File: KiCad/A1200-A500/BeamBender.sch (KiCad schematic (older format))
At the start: 17 parts, among them J1 4-1734742-0, J2 HDMI_A_1.4, J3 STX-3501-3N, U1 LM1117-3.3, U3 ADV7513BSWZ

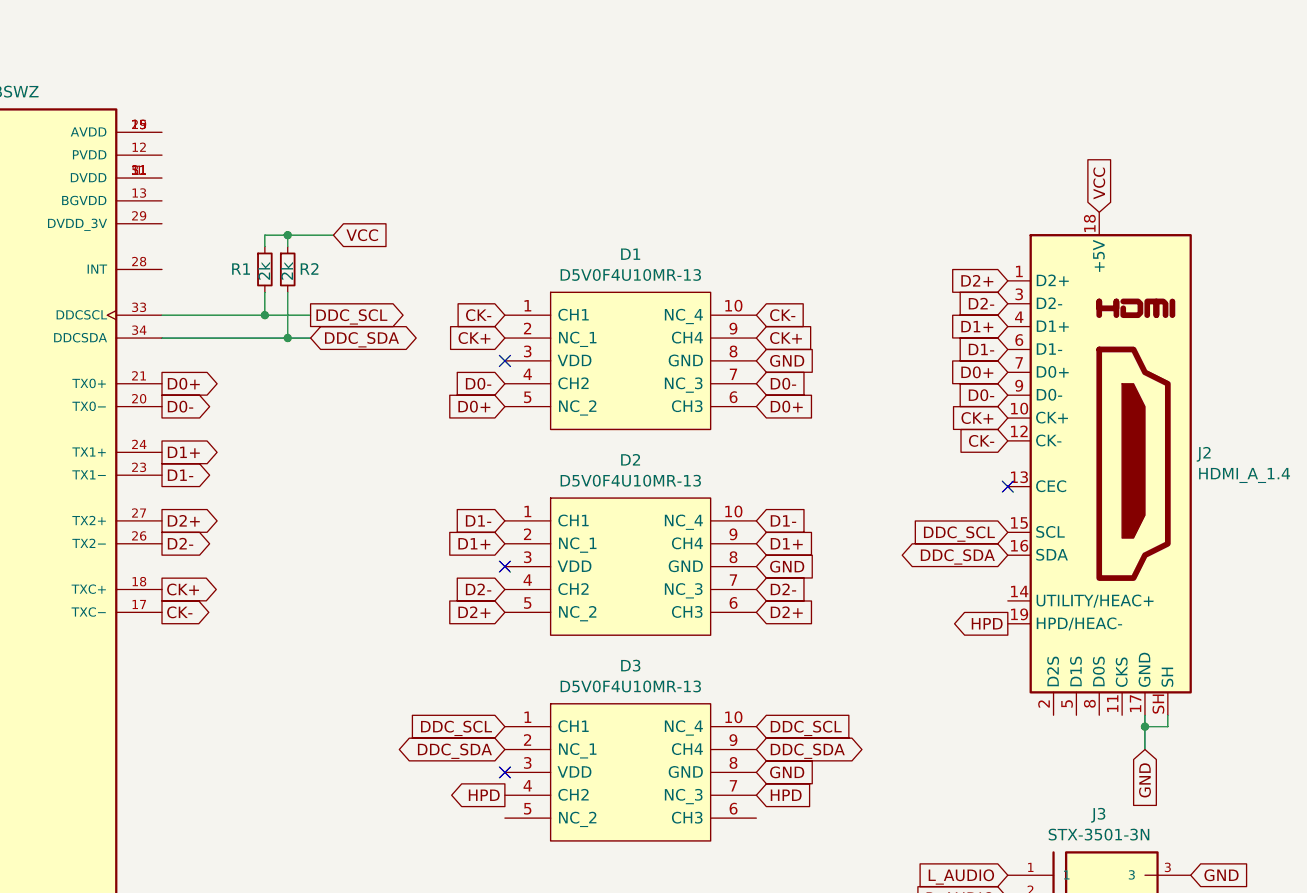
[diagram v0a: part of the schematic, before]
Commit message: more diff-pair routing
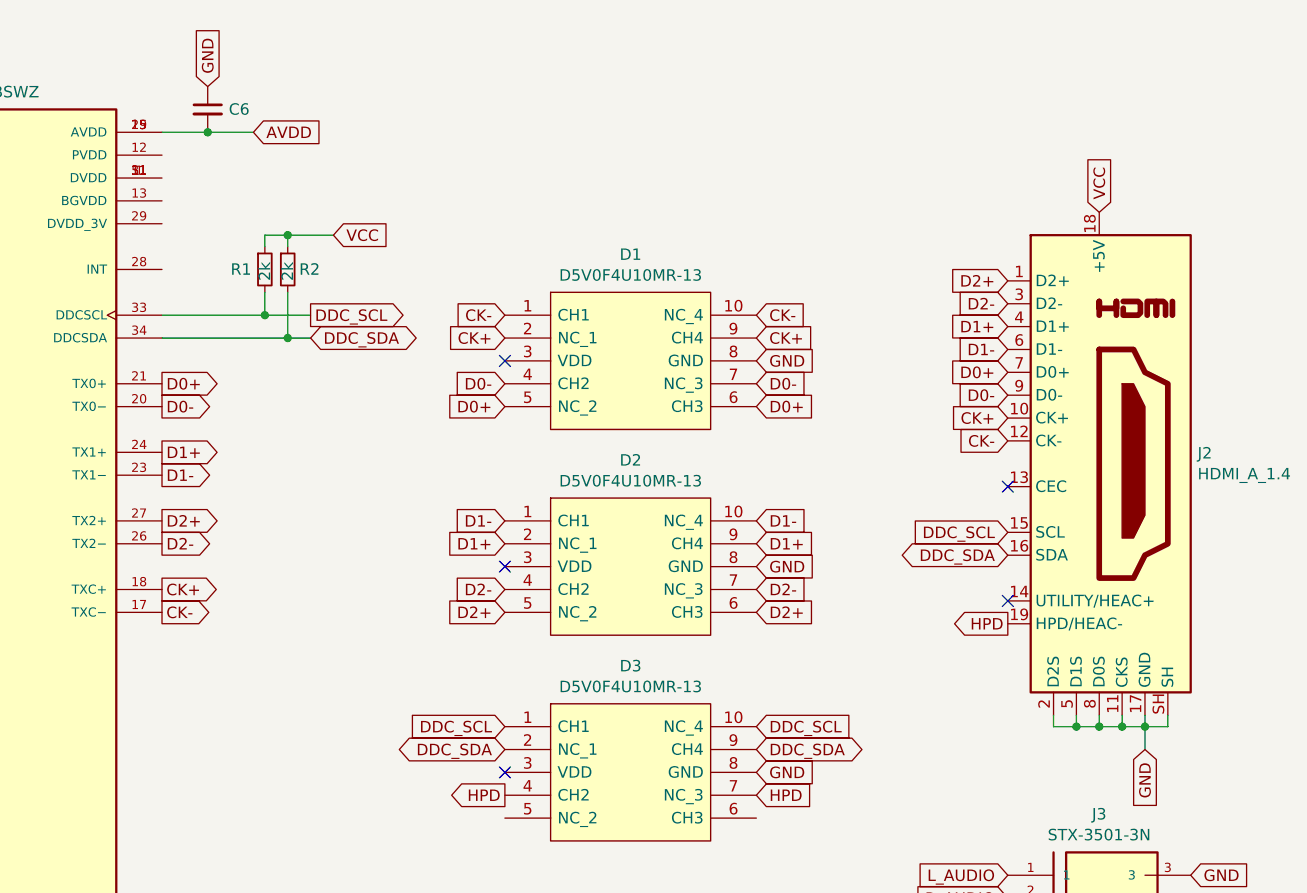
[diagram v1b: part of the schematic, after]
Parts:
- added C6: C_Small, Capacitor_SMD:C_0603_1608Metric_Pad1.08x0.95mm_HandSolder, symbol Device:C_Small
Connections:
- net GND: now also J2.11 (CKS), J2.2 (D2S), J2.5 (D1S), J2.8 (D0S), C6.1
- net AVDD: now reaches U3.15 (AVDD), U3.19 (AVDD), U3.25 (AVDD)
- net AVDD: now also C6.2
- no-connect marks 10 -> 11
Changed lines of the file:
@@
 Text GLabel 4400 5200 0    50   Input ~ 0
 R7_FPGA
+Wire Wire Line
+	9900 3450 9900 3500
+Wire Wire Line
+	9900 3500 10000 3500
+Wire Wire Line
+	10000 3450 10000 3500
+Connection ~ 10000 3500
+Wire Wire Line
+	10000 3500 10100 3500
+Wire Wire Line
+	10100 3450 10100 3500
+Connection ~ 10100 3500
+Wire Wire Line
+	10100 3500 10200 3500
+Wire Wire Line
+	10200 3450 10200 3500
+Connection ~ 10200 3500
+Wire Wire Line
+	10200 3500 10300 3500
+NoConn ~ 9700 2950
+Text GLabel 6400 900  2    50   Input ~ 0
+AVDD
+Wire Wire Line
+	6000 900  6200 900
+$Comp
+L Device:C_Small C6
+U 1 1 653C1DFE
+P 6200 800
+F 0 "C6" H 6292 800 50  0000 L CNN
+F 1 "C_Small" H 6292 755 50  0001 L CNN
+F 2 "Capacitor_SMD:C_0603_1608Metric_Pad1.08x0.95mm_HandSolder" H 6200 800 50  0001 C CNN
+F 3 "~" H 6200 800 50  0001 C CNN
+	1    6200 800
+	1    0    0    -1
+$EndComp
+Connection ~ 6200 900
+Wire Wire Line
+	6200 900  6400 900
+Text GLabel 6200 700  1    50   Input ~ 0
+GND
 $EndSCHEMATC

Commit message: more place and route
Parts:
- added C10, C11, C8, C9: 0.1uF, Capacitor_SMD:C_0603_1608Metric_Pad1.08x0.95mm_HandSolder, symbol Device:C_Small
- added C7: C_Small, Capacitor_SMD:C_0603_1608Metric_Pad1.08x0.95mm_HandSolder, symbol Device:C_Small
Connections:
- net labels added: Vp_D1, Vp_D2
- wire segments 58 -> 69
- no-connect marks 11 -> 10
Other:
- note added: "Central ESD clamp connected to VCC to \nalso provide protection for the VCC-line."
- note added: "ESD Protection"
- note added: "ESD bypass, \nThis limits any momentary voltage surge \nat the IO pin during the ESD strike event."
- moved on the sheet: D1, D2, D3
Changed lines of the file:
@@
 	1    0    0    -1
 $EndComp
-Text GLabel 10100 1250 1    50   Input ~ 0
+Text GLabel 10100 1150 2    50   Input ~ 0
 VCC
 Text GLabel 1150 2400 0    50   Input ~ 0
@@
 L BeamBender:D5V0F4U10MR-13 D1
 U 1 1 65246756
-P 8050 1900
-F 0 "D1" H 8050 2365 50  0000 C CNN
-F 1 "D5V0F4U10MR-13" H 8050 2274 50  0000 C CNN
-F 2 "BeamBender:SOP50P490X110-10N" H 8450 2200 50  0001 L CNN
-F 3 "" H 8450 2100 50  0001 L CNN
-	1    8050 1900
+P 8250 1800
+F 0 "D1" H 8250 1800 50  0000 C CNN
+F 1 "D5V0F4U10MR-13" H 8250 2174 50  0000 C CNN
+F 2 "BeamBender:SOP50P490X110-10N" H 8650 2100 50  0001 L CNN
+F 3 "" H 8650 2000 50  0001 L CNN
+	1    8250 1800
 	1    0    0    -1
 $EndComp
@@
 Text GLabel 6000 3000 2    50   Output ~ 0
 CK-
-Text GLabel 7500 1700 0    50   Input ~ 0
+Text GLabel 7700 1600 0    50   Input ~ 0
 CK-
-Text GLabel 7500 1800 0    50   Input ~ 0
+Text GLabel 7700 1700 0    50   Input ~ 0
 CK+
-Text GLabel 8600 1700 2    50   Input ~ 0
+Text GLabel 8800 1600 2    50   Input ~ 0
 CK-
-Text GLabel 8600 1800 2    50   Input ~ 0
+Text GLabel 8800 1700 2    50   Input ~ 0
 CK+
-Text GLabel 7500 2000 0    50   Input ~ 0
+Text GLabel 7700 1900 0    50   Input ~ 0
 D0-
-Text GLabel 7500 2100 0    50   Input ~ 0
+Text GLabel 7700 2000 0    50   Input ~ 0
 D0+
-Text GLabel 8600 2000 2    50   Input ~ 0
+Text GLabel 8800 1900 2    50   Input ~ 0
 D0-
-Text GLabel 8600 2100 2    50   Input ~ 0
+Text GLabel 8800 2000 2    50   Input ~ 0
 D0+
-NoConn ~ 7500 1900
-Text GLabel 8600 1900 2    50   Input ~ 0
+Text GLabel 8800 1800 2    50   Input ~ 0
 GND
 Text GLabel 9700 2250 0    50   Input ~ 0
@@
 L BeamBender:D5V0F4U10MR-13 D2
 U 1 1 652A2640
-P 8050 2800
-F 0 "D2" H 8050 3265 50  0000 C CNN
-F 1 "D5V0F4U10MR-13" H 8050 3174 50  0000 C CNN
-F 2 "BeamBender:SOP50P490X110-10N" H 8450 3100 50  0001 L CNN
-F 3 "" H 8450 3000 50  0001 L CNN
-	1    8050 2800
-	1    0    0    -1
-$EndComp
-Text GLabel 7500 2600 0    50   Input ~ 0
+P 8250 2800
+F 0 "D2" H 8250 2800 50  0000 C CNN
+F 1 "D5V0F4U10MR-13" H 8250 3174 50  0000 C CNN
+F 2 "BeamBender:SOP50P490X110-10N" H 8650 3100 50  0001 L CNN
+F 3 "" H 8650 3000 50  0001 L CNN
+	1    8250 2800
+	1    0    0    -1
+$EndComp
+Text GLabel 7700 2600 0    50   Input ~ 0
 D1-
-Text GLabel 7500 2700 0    50   Input ~ 0
+Text GLabel 7700 2700 0    50   Input ~ 0
 D1+
-Text GLabel 7500 2900 0    50   Input ~ 0
+Text GLabel 7700 2900 0    50   Input ~ 0
 D2-
-Text GLabel 7500 3000 0    50   Input ~ 0
+Text GLabel 7700 3000 0    50   Input ~ 0
 D2+
-Text GLabel 8600 2600 2    50   Input ~ 0
+Text GLabel 8800 2600 2    50   Input ~ 0
 D1-
-Text GLabel 8600 2700 2    50   Input ~ 0
+Text GLabel 8800 2700 2    50   Input ~ 0
 D1+
-Text GLabel 8600 2900 2    50   Input ~ 0
+Text GLabel 8800 2900 2    50   Input ~ 0
 D2-
-Text GLabel 8600 3000 2    50   Input ~ 0
+Text GLabel 8800 3000 2    50   Input ~ 0
 D2+
-Text GLabel 8600 2800 2    50   Input ~ 0
-GND
-NoConn ~ 7500 2800
+Text GLabel 8800 2800 2    50   Input ~ 0
+GND
 Text GLabel 9700 1850 0    50   Input ~ 0
 D1-
@@
 L BeamBender:D5V0F4U10MR-13 D3
 U 1 1 652AB064
-P 8050 3700
-F 0 "D3" H 8050 4165 50  0000 C CNN
-F 1 "D5V0F4U10MR-13" H 8050 4074 50  0000 C CNN
-F 2 "BeamBender:SOP50P490X110-10N" H 8450 4000 50  0001 L CNN
-F 3 "" H 8450 3900 50  0001 L CNN
-	1    8050 3700
+P 8250 3700
+F 0 "D3" H 8250 4165 50  0000 C CNN
+F 1 "D5V0F4U10MR-13" H 8250 4074 50  0000 C CNN
+F 2 "BeamBender:SOP50P490X110-10N" H 8650 4000 50  0001 L CNN
+F 3 "" H 8650 3900 50  0001 L CNN
+	1    8250 3700
 	1    0    0    -1
 $EndComp
 Text GLabel 9700 3050 0    50   Output ~ 0
 HPD
-Text GLabel 7500 3800 0    50   Output ~ 0
+Text GLabel 7700 3600 0    50   Output ~ 0
 HPD
-Text GLabel 8600 3800 2    50   Input ~ 0
+Text GLabel 8800 3600 2    50   Input ~ 0
 HPD
 Text GLabel 3700 5700 0    50   Input ~ 0
@@
 Text GLabel 9700 2750 0    50   BiDi ~ 0
 DDC_SDA
-Text GLabel 7500 3500 0    50   Input ~ 0
+Text GLabel 7700 3900 0    50   Input ~ 0
 DDC_SCL
-Text GLabel 8600 3500 2    50   Input ~ 0
+Text GLabel 8800 3900 2    50   Input ~ 0
 DDC_SCL
-Text GLabel 7500 3600 0    50   BiDi ~ 0
+Text GLabel 7700 3800 0    50   BiDi ~ 0
 DDC_SDA
-Text GLabel 8600 3600 2    50   BiDi ~ 0
+Text GLabel 8800 3800 2    50   BiDi ~ 0
 DDC_SDA
-Text GLabel 8600 3700 2    50   Input ~ 0
-GND
-NoConn ~ 7500 3700
+Text GLabel 8800 3700 2    50   Input ~ 0
+GND
 $Comp
 L Device:R_Small R2
@@
 	10200 3500 10300 3500
 NoConn ~ 9700 2950
-Text GLabel 6400 900  2    50   Input ~ 0
+Text GLabel 6750 900  2    50   Input ~ 0
 AVDD
 Wire Wire Line
@@
 U 1 1 653C1DFE
 P 6200 800
-F 0 "C6" H 6292 800 50  0000 L CNN
+F 0 "C6" H 6000 900 50  0000 L CNN
 F 1 "C_Small" H 6292 755 50  0001 L CNN
 F 2 "Capacitor_SMD:C_0603_1608Metric_Pad1.08x0.95mm_HandSolder" H 6200 800 50  0001 C CNN
@@
 $EndComp
 Connection ~ 6200 900
-Wire Wire Line
-	6200 900  6400 900
 Text GLabel 6200 700  1    50   Input ~ 0
 GND
+Wire Wire Line
+	6200 900  6350 900
+$Comp
+L Device:C_Small C7
+U 1 1 653F698E
+P 6350 800
+F 0 "C7" H 6400 900 50  0000 L CNN
+F 1 "C_Small" H 6442 755 50  0001 L CNN
+F 2 "Capacitor_SMD:C_0603_1608Metric_Pad1.08x0.95mm_HandSolder" H 6350 800 50  0001 C CNN
+F 3 "~" H 6350 800 50  0001 C CNN
+	1    6350 800
+	1    0    0    -1
+$EndComp
+Connection ~ 6350 900
+Wire Wire Line
+	6350 900  6750 900
+Wire Wire Line
+	6200 700  6350 700
+Text GLabel 7200 3850 0    50   Input ~ 0
+VCC
+NoConn ~ 7700 3500
+NoConn ~ 8800 3500
+Wire Wire Line
+	7700 2800 7350 2800
+$Comp
+L Device:C_Small C9
+U 1 1 65476445
+P 7350 2700
+F 0 "C9" H 7150 2700 50  0000 L CNN
+F 1 "0.1uF" H 7442 2655 50  0001 L CNN
+F 2 "Capacitor_SMD:C_0603_1608Metric_Pad1.08x0.95mm_HandSolder" H 7350 2700 50  0001 C CNN
+F 3 "~" H 7350 2700 50  0001 C CNN
+	1    7350 2700
+	1    0    0    -1
+$EndComp
+$Comp
+L Device:C_Small C8
+U 1 1 6547758E
+P 7350 1900
+F 0 "C8" H 7150 1900 50  0000 L CNN
+F 1 "0.1uF" H 7442 1855 50  0001 L CNN
+F 2 "Capacitor_SMD:C_0603_1608Metric_Pad1.08x0.95mm_HandSolder" H 7350 1900 50  0001 C CNN
+F 3 "~" H 7350 1900 50  0001 C CNN
+	1    7350 1900
+	1    0    0    -1
+$EndComp
+Wire Notes Line
+	7100 1150 9250 1150
+Text Notes 7650 1300 0    100  ~ 0
+ESD Protection
+Wire Wire Line
+	7700 1800 7350 1800
+$Comp
+L Device:C_Small C10
+U 1 1 6548D3D3
+P 7350 3600
+F 0 "C10" H 7100 3600 50  0000 L CNN
+F 1 "0.1uF" H 7442 3555 50  0001 L CNN
+F 2 "Capacitor_SMD:C_0603_1608Metric_Pad1.08x0.95mm_HandSolder" H 7350 3600 50  0001 C CNN
+F 3 "~" H 7350 3600 50  0001 C CNN
+	1    7350 3600
+	1    0    0    -1
+$EndComp
+Wire Wire Line
+	7200 3700 7350 3700
+Connection ~ 7350 3700
+Wire Wire Line
+	7350 3700 7700 3700
+Text GLabel 7350 2350 0    50   Input ~ 0
+GND
+Text GLabel 7350 3500 1    50   Input ~ 0
+GND
+Wire Wire Line
+	7350 2000 7350 2200
+Text Notes 7400 2300 0    50   ~ 0
+ESD bypass, \nThis limits any momentary voltage surge \nat the IO pin during the ESD strike event.
+Wire Wire Line
+	7350 2200 7400 2200
+Connection ~ 7350 2200
+Wire Wire Line
+	7350 2200 7350 2600
+Text Notes 7150 4200 0    50   ~ 0
+Central ESD clamp connected to VCC to \nalso provide protection for the VCC-line.
+Wire Notes Line
+	7100 4350 9250 4350
+Wire Notes Line
+	9250 1150 9250 4350
+Wire Notes Line
+	7100 1150 7100 4350
+Wire Wire Line
+	7200 3700 7200 4000
+Text Label 7350 2800 2    50   ~ 0
+Vp_D2
+Text Label 7350 1800 2    50   ~ 0
+Vp_D1
+$Comp
+L Device:C_Small C11
+U 1 1 654A833A
+P 10100 1000
+F 0 "C11" H 9850 1000 50  0000 L CNN
+F 1 "0.1uF" H 10192 955 50  0001 L CNN
+F 2 "Capacitor_SMD:C_0603_1608Metric_Pad1.08x0.95mm_HandSolder" H 10100 1000 50  0001 C CNN
+F 3 "~" H 10100 1000 50  0001 C CNN
+	1    10100 1000
+	1    0    0    -1
+$EndComp
+Text GLabel 10100 900  1    50   Input ~ 0
+GND
+Wire Wire Line
+	10100 1100 10100 1250
 $EndSCHEMATC

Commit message: more place and route
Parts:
- added C12: 10uF, Capacitor_SMD:C_1206_3216Metric_Pad1.33x1.80mm_HandSolder, symbol Device:C_Small
- C6, C7: value C_Small -> 0.1uF
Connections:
- wire segments 69 -> 71
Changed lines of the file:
@@
 	1    0    0    -1
 $EndComp
-Text GLabel 10100 1150 2    50   Input ~ 0
+Text GLabel 10650 1100 2    50   Input ~ 0
 VCC
 Text GLabel 1150 2400 0    50   Input ~ 0
@@
 P 6200 800
 F 0 "C6" H 6000 900 50  0000 L CNN
-F 1 "C_Small" H 6292 755 50  0001 L CNN
+F 1 "0.1uF" H 5900 800 50  0000 L CNN
 F 2 "Capacitor_SMD:C_0603_1608Metric_Pad1.08x0.95mm_HandSolder" H 6200 800 50  0001 C CNN
 F 3 "~" H 6200 800 50  0001 C CNN
@@
 P 6350 800
 F 0 "C7" H 6400 900 50  0000 L CNN
-F 1 "C_Small" H 6442 755 50  0001 L CNN
+F 1 "0.1uF" H 6450 800 50  0000 L CNN
 F 2 "Capacitor_SMD:C_0603_1608Metric_Pad1.08x0.95mm_HandSolder" H 6350 800 50  0001 C CNN
 F 3 "~" H 6350 800 50  0001 C CNN
@@
 Text GLabel 7350 3500 1    50   Input ~ 0
 GND
-Wire Wire Line
-	7350 2000 7350 2200
 Text Notes 7400 2300 0    50   ~ 0
 ESD bypass, \nThis limits any momentary voltage surge \nat the IO pin during the ESD strike event.
-Wire Wire Line
-	7350 2200 7400 2200
-Connection ~ 7350 2200
-Wire Wire Line
-	7350 2200 7350 2600
 Text Notes 7150 4200 0    50   ~ 0
 Central ESD clamp connected to VCC to \nalso provide protection for the VCC-line.
@@
 Wire Notes Line
 	7100 1150 7100 4350
-Wire Wire Line
-	7200 3700 7200 4000
 Text Label 7350 2800 2    50   ~ 0
 Vp_D2
@@
 U 1 1 654A833A
 P 10100 1000
-F 0 "C11" H 9850 1000 50  0000 L CNN
-F 1 "0.1uF" H 10192 955 50  0001 L CNN
+F 0 "C11" H 9850 1100 50  0000 L CNN
+F 1 "0.1uF" H 9800 1000 50  0000 L CNN
 F 2 "Capacitor_SMD:C_0603_1608Metric_Pad1.08x0.95mm_HandSolder" H 10100 1000 50  0001 C CNN
 F 3 "~" H 10100 1000 50  0001 C CNN
@@
 	1    0    0    -1
 $EndComp
-Text GLabel 10100 900  1    50   Input ~ 0
+Text GLabel 10100 800  1    50   Input ~ 0
 GND
 Wire Wire Line
 	10100 1100 10100 1250
+Wire Wire Line
+	10100 800  10100 900
+Wire Wire Line
+	10100 900  10300 900
+Connection ~ 10100 900
+Connection ~ 10100 1100
+Wire Wire Line
+	7200 3700 7200 3850
+Wire Wire Line
+	7350 2000 7350 2600
+$Comp
+L Device:C_Small C12
+U 1 1 654D36E6
+P 10300 1000
+F 0 "C12" H 10392 1046 50  0000 L CNN
+F 1 "10uF" H 10392 955 50  0000 L CNN
+F 2 "Capacitor_SMD:C_1206_3216Metric_Pad1.33x1.80mm_HandSolder" H 10300 1000 50  0001 C CNN
+F 3 "~" H 10300 1000 50  0001 C CNN
+	1    10300 1000
+	1    0    0    -1
+$EndComp
+Wire Wire Line
+	10100 1100 10300 1100
+Connection ~ 10300 1100
+Wire Wire Line
+	10300 1100 10650 1100
 $EndSCHEMATC

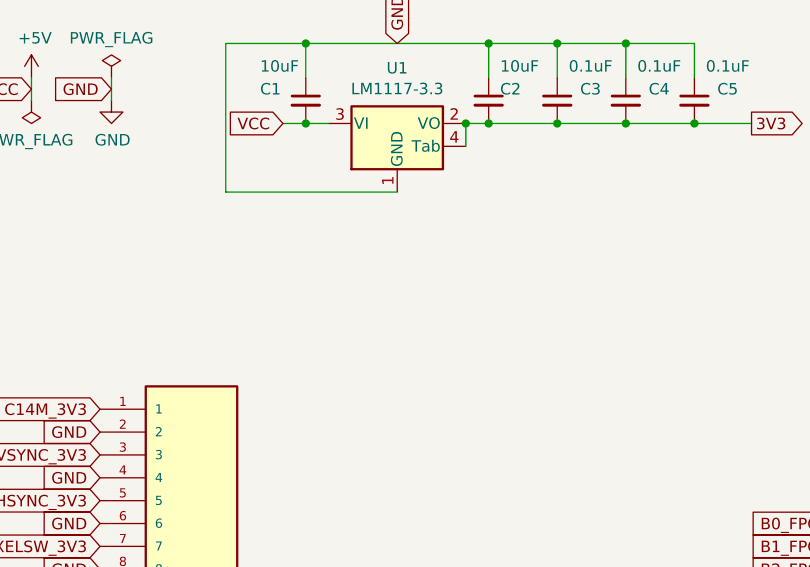
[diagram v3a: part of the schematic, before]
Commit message: Added a Phoenix Contact for +5V power supply and did some place and route around the 3.3V-regulator
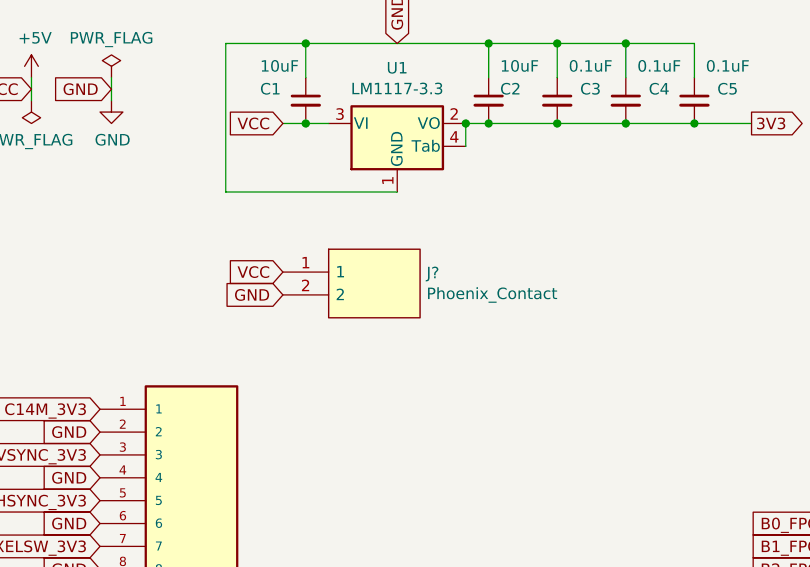
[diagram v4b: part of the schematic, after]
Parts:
- added J?: Phoenix_Contact, BeamBender:Phoenix_Contact, symbol BeamBender:Phoenix_Contact
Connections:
- net +5V: now also J?.1
- net GND: now also J?.2
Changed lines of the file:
@@
 Wire Wire Line
 	10300 1100 10650 1100
+$Comp
+L BeamBender:Phoenix_Contact J?
+U 1 1 654E9506
+P 2350 1850
+F 0 "J?" H 2578 1896 50  0000 L CNN
+F 1 "Phoenix_Contact" H 2578 1805 50  0000 L CNN
+F 2 "BeamBender:Phoenix_Contact" H 2600 2000 50  0001 L CNN
+F 3 "" H 2600 1900 50  0001 L CNN
+	1    2350 1850
+	1    0    0    -1
+$EndComp
+Text GLabel 1950 1800 0    50   Input ~ 0
+VCC
+Text GLabel 1950 1900 0    50   Input ~ 0
+GND
 $EndSCHEMATC
